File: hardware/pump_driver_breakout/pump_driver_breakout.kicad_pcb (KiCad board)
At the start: 2 copper layers, 40 x 30 mm, 18 parts, among them J1 DC IN, J2 CONTROL, J3 Motor, Q1 PSMN011-30YLC

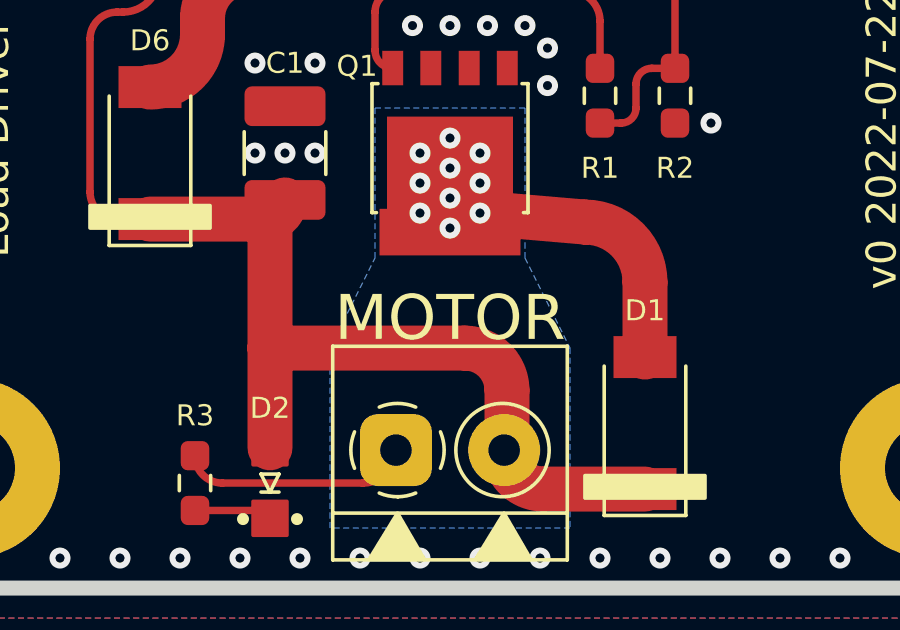
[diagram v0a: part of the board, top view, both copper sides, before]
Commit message: Add smart solenoid drivers
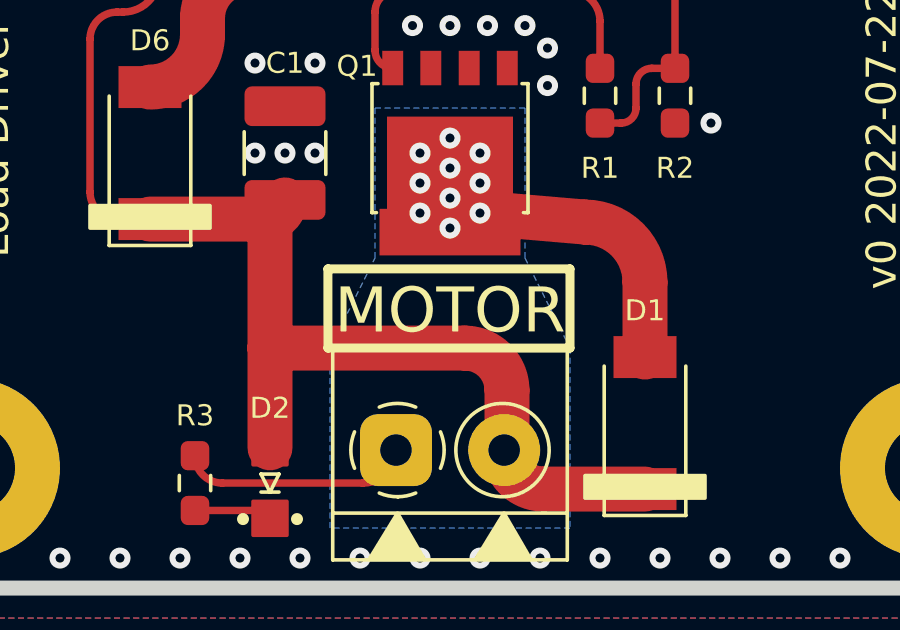
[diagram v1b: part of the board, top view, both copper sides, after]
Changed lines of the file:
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@@
   (gr_rect (start 87.91 89.275) (end 81.09 87.135) (layer "F.SilkS") (width 0.3) (fill none))
   (gr_rect (start 77.5 96.325) (end 81.5 97.075) (layer "F.SilkS") (width 0.12) (fill solid))
+  (gr_rect (start 93.5 101.075) (end 85.43 98.435) (layer "F.SilkS") (width 0.3) (fill none))
   (gr_rect (start 97.91 89.275) (end 91.09 87.135) (layer "F.SilkS") (width 0.3) (fill none))
   (gr_line (start 89.5 77.075) (end 89.5 111.075) (layer "Cmts.User") (width 0.1))
@@
     (effects (font (size 1 1) (thickness 0.2)) (justify mirror))
   )
-  (gr_text "MOTOR" (at 89.5 100.075) (layer "F.SilkS")
+  (gr_text "MOTOR" (at 89.5 99.825) (layer "F.SilkS")
     (effects (font (size 1.5 1.5) (thickness 0.3)))
   )
